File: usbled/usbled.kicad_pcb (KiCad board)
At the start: 2 copper layers, 25 x 12.1 mm, 5 parts, among them J1 USB_A

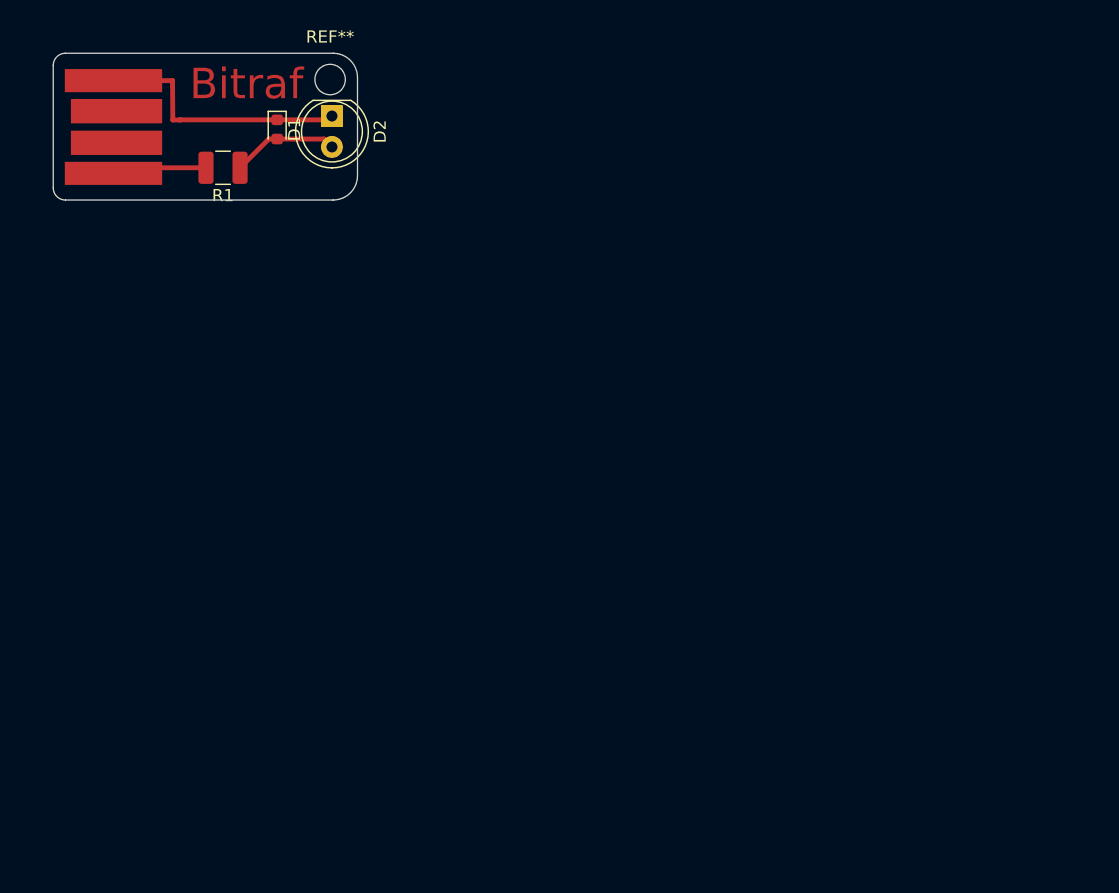
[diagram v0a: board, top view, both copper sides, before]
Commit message: usbled: Export Gerbers for 3x boards
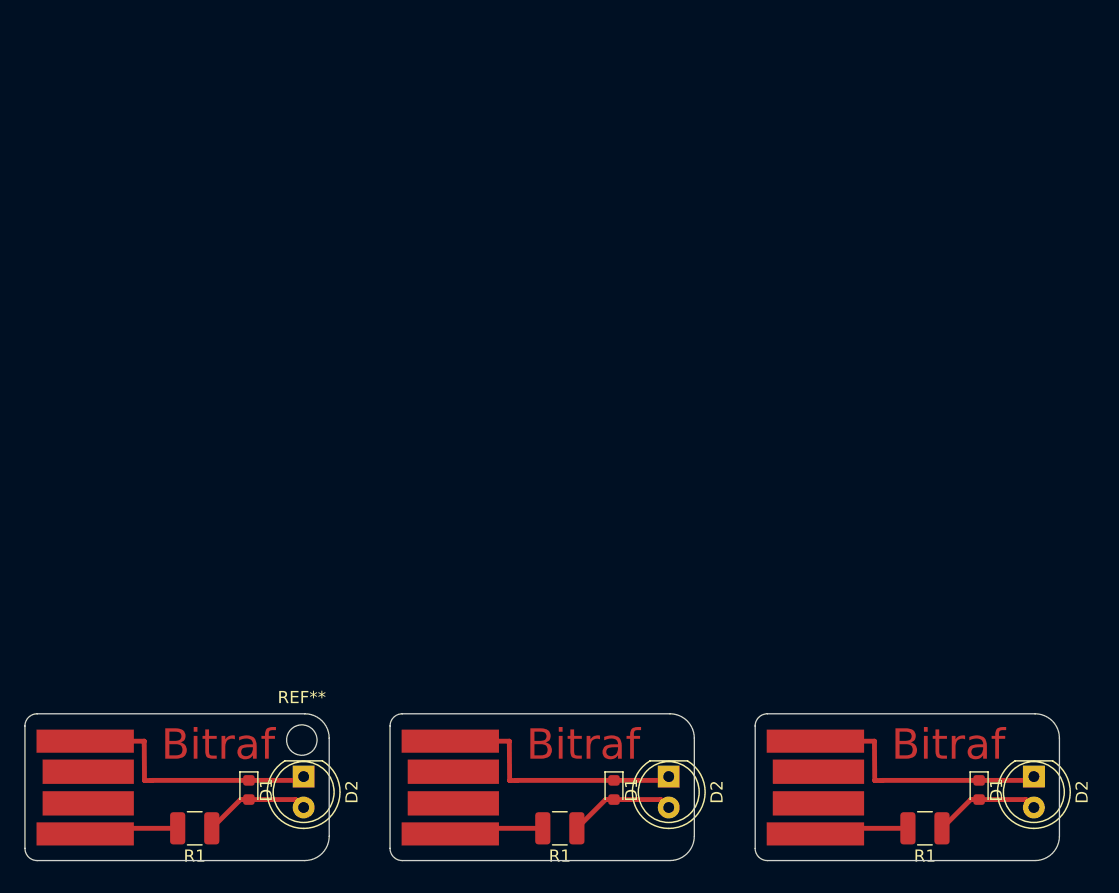
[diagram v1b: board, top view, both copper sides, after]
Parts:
- removed the D1 at (122.2, 39.1)
- removed the D2 at (126.7, 38.0)
- removed the J1 at (103.8, 38.9)
- removed the R1 at (117.7, 42.2)
- added D1: LED SMD, LED_SMD:LED_0603_1608Metric, F.Cu at (179.8, 93.4)
- added D1: LED SMD, LED_SMD:LED_0603_1608Metric, F.Cu at (149.8, 93.4)
- added D1: LED SMD, LED_SMD:LED_0603_1608Metric, F.Cu at (119.8, 93.4)
- added D2: LED, LED_THT:LED_D5.0mm, F.Cu at (184.3, 92.3)
- added D2: LED, LED_THT:LED_D5.0mm, F.Cu at (154.3, 92.3)
- added D2: LED, LED_THT:LED_D5.0mm, F.Cu at (124.3, 92.3)
- added J1: USB_A, usbled:usb-pcb, F.Cu at (161.5, 93.2)
- added J1: USB_A, usbled:usb-pcb, F.Cu at (131.5, 93.2)
- added J1: USB_A, usbled:usb-pcb, F.Cu at (101.5, 93.2)
- added R1: 470, Resistor_SMD:R_1210_3225Metric, F.Cu at (175.4, 96.5)
- added R1: 470, Resistor_SMD:R_1210_3225Metric, F.Cu at (145.4, 96.5)
- added R1: 470, Resistor_SMD:R_1210_3225Metric, F.Cu at (115.4, 96.5)
- moved REF** 54.3 mm to (124.2, 89.3)
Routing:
- net GND: track 21.3 -> 63.9 mm
- net Net-(D1-Pad2): track 8.80 -> 26.4 mm
- net +5V: track 7.79 -> 23.4 mm
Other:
- board size 25 x 12.1 mm -> 85 x 12.1 mm

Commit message: usbled: Update and partial CAM setup
Fighting with FlatCAM regarding the outlines
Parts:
- added REF**: MountingHole_2.5mm, MountingHole:MountingHole_2.5mm, F.Cu at (184.2, 89.3)
- added REF**: MountingHole_2.5mm, MountingHole:MountingHole_2.5mm, F.Cu at (154.2, 89.3)
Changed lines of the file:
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@@
     (tracks 39)
     (zones 0)
-    (modules 13)
+    (modules 15)
     (nets 6)
   )
@@
     (pad_to_mask_clearance 0.051)
     (solder_mask_min_width 0.25)
-    (aux_axis_origin 0 0)
+    (aux_axis_origin 101.475 99.175)
     (visible_elements FFFFFF7F)
     (pcbplotparams
@@
       (viasonmask false)
       (mode 1)
-      (useauxorigin false)
+      (useauxorigin true)
       (hpglpennumber 1)
       (hpglpenspeed 20)
@@
       (outputformat 1)
       (mirror false)
-      (drillshape 1)
+      (drillshape 0)
       (scaleselection 1)
-      (outputdirectory ""))
+      (outputdirectory "./out"))
   )
   (net 0 "")
@@
     )
   )
+  (module MountingHole:MountingHole_2.5mm (layer F.Cu)
+    (at 184.175 89.275)
+    (descr "Mounting Hole 2.5mm, no annular")
+    (tags "mounting hole 2.5mm no annular")
+    (attr virtual)
+    (fp_text reference REF** (at 0 -3.5) (layer F.SilkS)
+      (effects (font (size 1 1) (thickness 0.15)))
+    )
+    (fp_text value MountingHole_2.5mm (at 0 3.5) (layer F.Fab)
+      (effects (font (size 1 1) (thickness 0.15)))
+    )
+    (fp_circle (center 0 0) (end 2.75 0) (layer F.CrtYd) (width 0.05))
+    (fp_circle (center 0 0) (end 2.5 0) (layer Cmts.User) (width 0.15))
+    (fp_text user %R (at 0.3 0) (layer F.Fab)
+      (effects (font (size 1 1) (thickness 0.15)))
+    )
+    (pad 1 np_thru_hole circle (at 0 0) (size 2.5 2.5) (drill 2.5) (layers *.Cu *.Mask))
+  )
+  (module MountingHole:MountingHole_2.5mm (layer F.Cu)
+    (at 154.175 89.275)
+    (descr "Mounting Hole 2.5mm, no annular")
+    (tags "mounting hole 2.5mm no annular")
+    (attr virtual)
+    (fp_text reference REF** (at 0 -3.5) (layer F.SilkS)
+      (effects (font (size 1 1) (thickness 0.15)))
+    )
+    (fp_text value MountingHole_2.5mm (at 0 3.5) (layer F.Fab)
+      (effects (font (size 1 1) (thickness 0.15)))
+    )
+    (fp_circle (center 0 0) (end 2.75 0) (layer F.CrtYd) (width 0.05))
+    (fp_circle (center 0 0) (end 2.5 0) (layer Cmts.User) (width 0.15))
+    (fp_text user %R (at 0.3 0) (layer F.Fab)
+      (effects (font (size 1 1) (thickness 0.15)))
+    )
+    (pad 1 np_thru_hole circle (at 0 0) (size 2.5 2.5) (drill 2.5) (layers *.Cu *.Mask))
+  )
   (module LED_SMD:LED_0603_1608Metric (layer F.Cu)
     (at 179.825 93.375 270)
@@
   (gr_arc (start 184.425 97.175) (end 184.425 99.175) (angle -90) (layer Edge.Cuts) (width 0.1))
   (gr_arc (start 154.425 97.175) (end 154.425 99.175) (angle -90) (layer Edge.Cuts) (width 0.1))
+  (gr_line (start 200 100) (end 100 100) (layer Eco1.User) (width 0.1))
   (gr_arc (start 102.425 88.115) (end 102.425 87.115) (angle -90) (layer Edge.Cuts) (width 0.1))
   (gr_line (start 126.425 89.115) (end 126.425 97.175) (layer Edge.Cuts) (width 0.1))
@@
   (gr_line (start 200 25) (end 200 100) (layer Eco1.User) (width 0.1))
   (gr_line (start 100 100) (end 100 25) (layer Eco1.User) (width 0.1))
-  (gr_line (start 200 100) (end 100 100) (layer Eco1.User) (width 0.1))
   (gr_line (start 100 25) (end 200 25) (layer Eco1.User) (width 0.1))
   (segment (start 124.0125 92.5875) (end 124.325 92.275) (width 0.4) (layer F.Cu) (net 1))
